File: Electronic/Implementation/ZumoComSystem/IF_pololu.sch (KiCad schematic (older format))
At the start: 4 parts, among them J3 Conn_02x13_Odd_Even, J4 Conn_02x13_Odd_Even, J5 Conn_02x07_Odd_Even, J6 Conn_02x07_Odd_Even

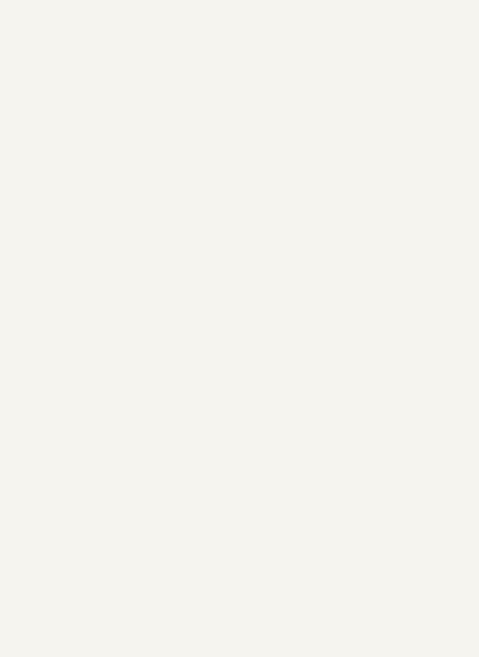
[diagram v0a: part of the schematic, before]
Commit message: electronic -> Schematic -> add hierarchical pins, modified Regulator page
           -> BOM & Clac: add new inductors
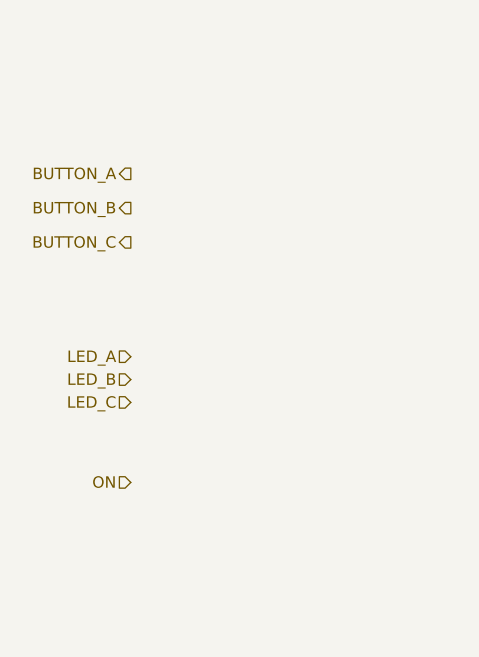
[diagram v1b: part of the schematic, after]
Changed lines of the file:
@@
 	1    0    0    -1
 $EndComp
+Text HLabel 2350 2900 0    50   Output ~ 0
+BUTTON_A
+Text HLabel 2350 3050 0    50   Output ~ 0
+BUTTON_B
+Text HLabel 2350 3200 0    50   Output ~ 0
+BUTTON_C
+Text HLabel 2350 3700 0    50   Input ~ 0
+LED_A
+Text HLabel 2350 3800 0    50   Input ~ 0
+LED_B
+Text HLabel 2350 3900 0    50   Input ~ 0
+LED_C
+Text HLabel 2350 4250 0    50   Input ~ 0
+ON
 $EndSCHEMATC

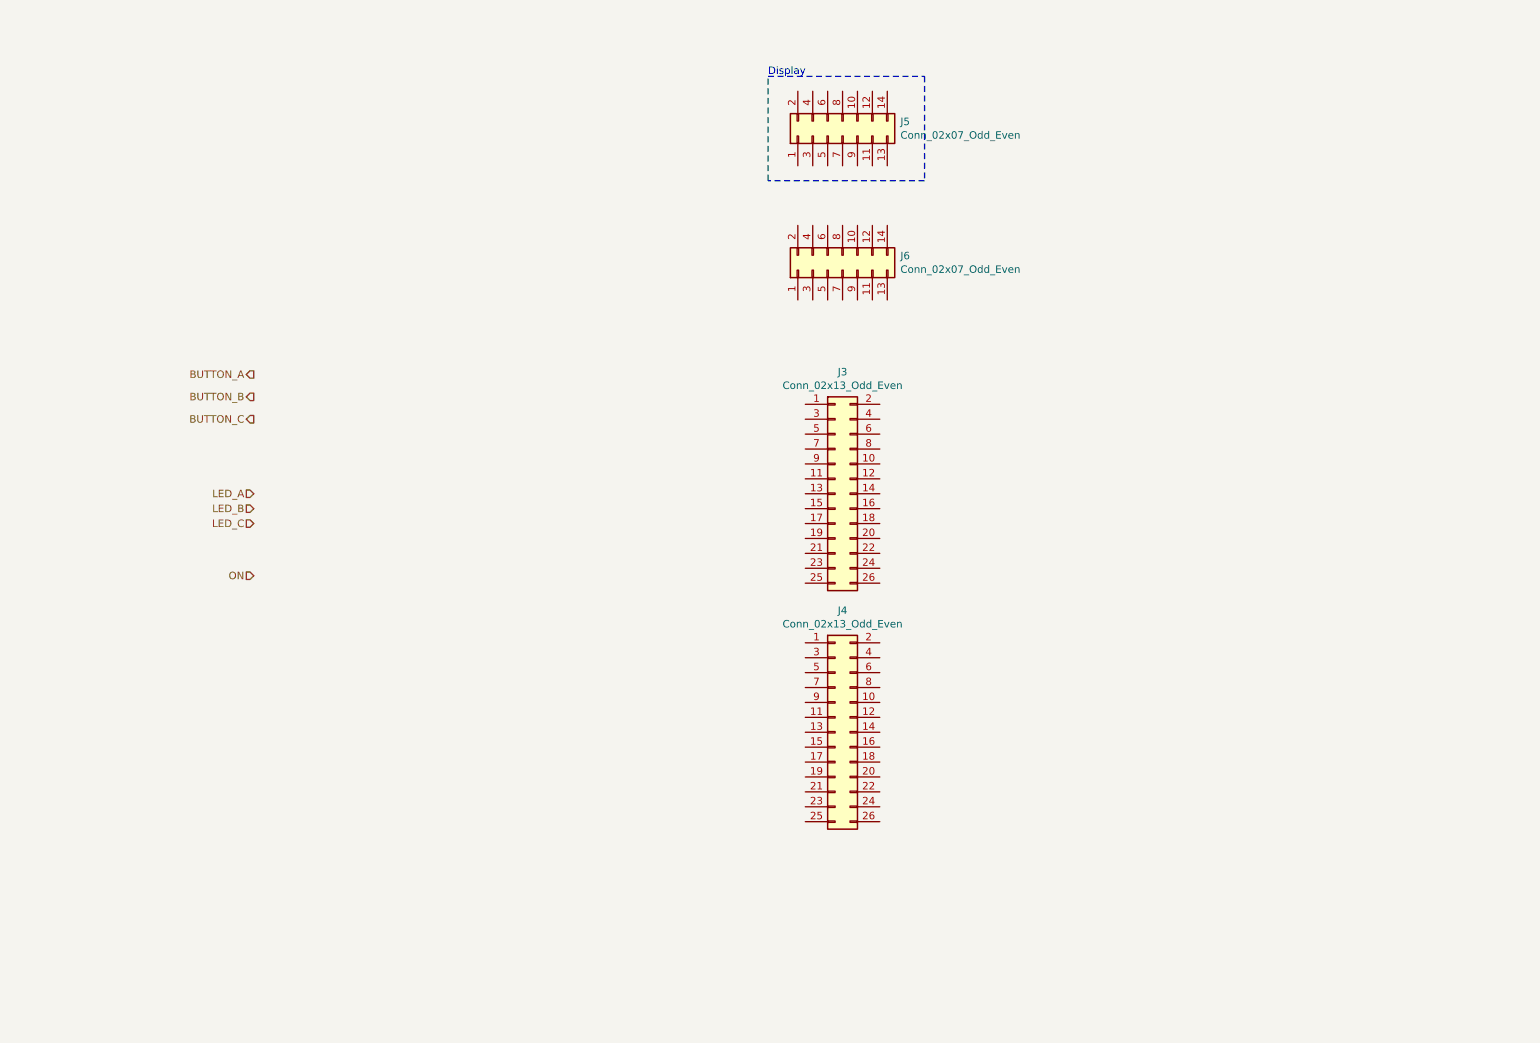
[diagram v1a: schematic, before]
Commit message: Electronic: Schematic: ESP I/Os, IF_Pololu Pins, USB_max
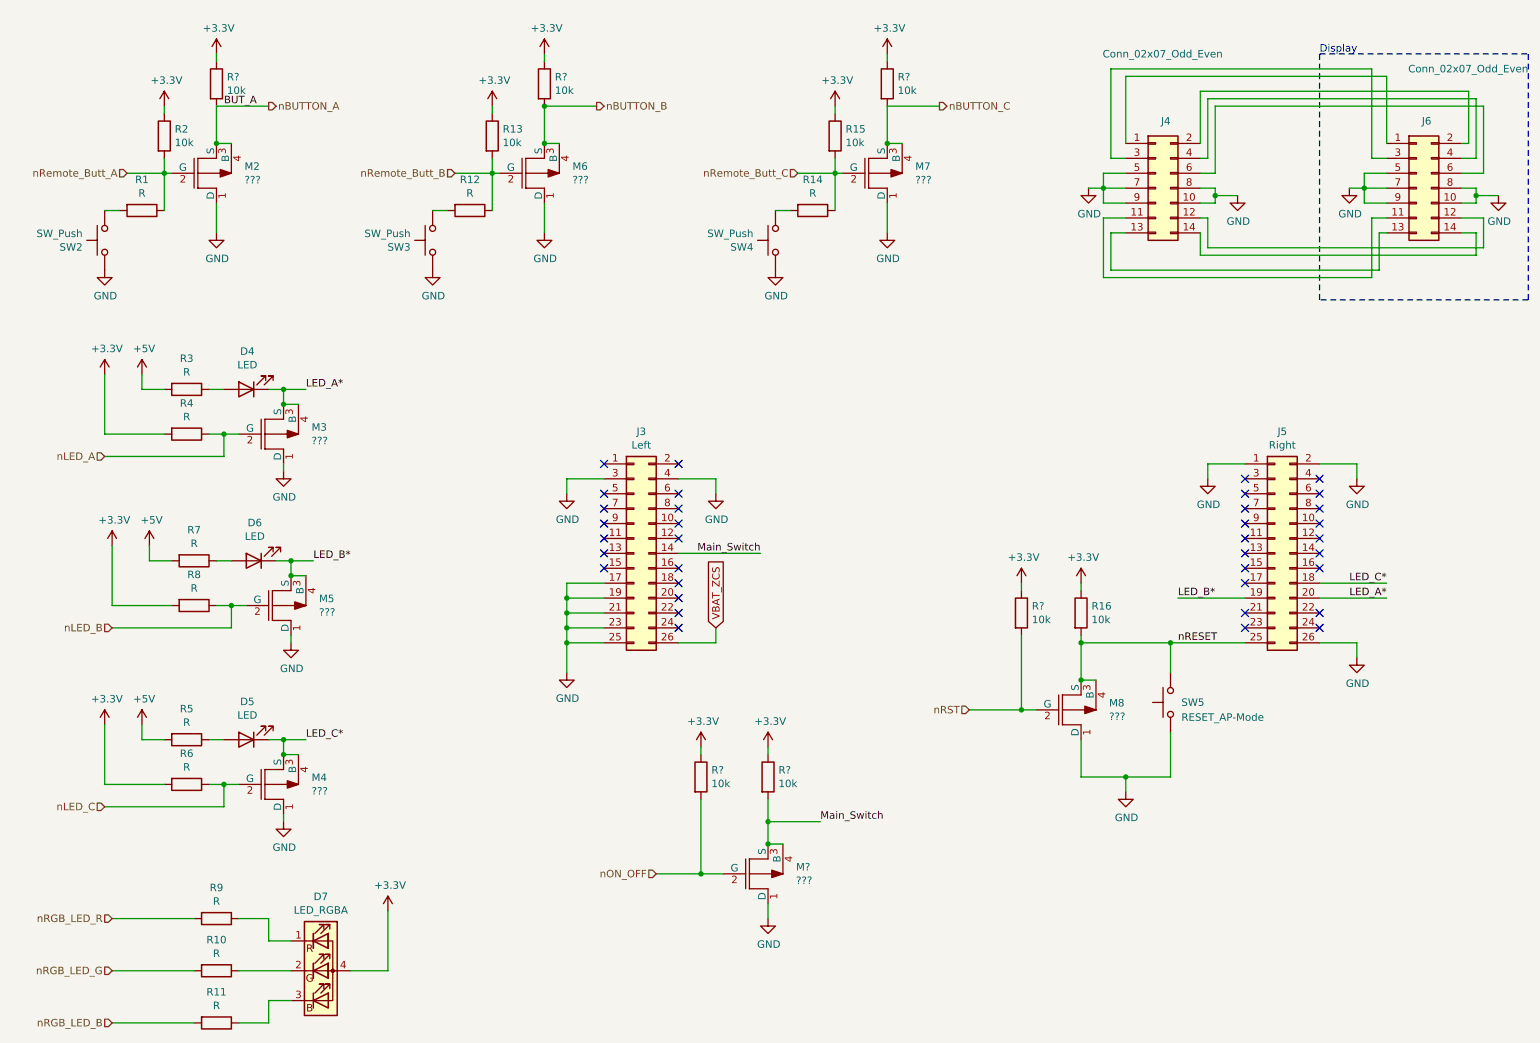
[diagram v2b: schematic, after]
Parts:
- added D4, D5, D6: LED, symbol Device:LED
- added D7: LED_RGBA, LED_SMD:LED_RGB_1210, symbol Device:LED_RGBA
- added M2, M3, M4, M5, M6, M7, M8, M?: ???, symbol pspice:MPMOS
- added R1, R10, R11, R12, R14, R3, R4, R5, R6, R7, R8, R9: R, symbol Device:R
- added R13, R15, R16, R2, R? (x6): 10k, symbol Device:R
- added SW2, SW3, SW4: SW_Push, symbol Switch:SW_Push
- added SW5: RESET_AP-Mode, Button_Switch_SMD:SW_SPST_TL3342, symbol Switch:SW_Push
- J3: value Conn_02x13_Odd_Even -> Left; footprint Connector_PinHeader_2.54mm:PinHeader_2x13_P2.54mm_Vertical -> Connector_PinHeader_2.54mm:PinHeader_2x13_P2.54mm_Vertical_SMD
- J5: renamed from J4; value Conn_02x13_Odd_Even -> Right; footprint Connector_PinHeader_2.54mm:PinHeader_2x13_P2.54mm_Vertical -> Connector_PinHeader_2.54mm:PinHeader_2x13_P2.54mm_Vertical_SMD
- renumbered J6 to J4, J5 to J6
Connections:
- net at J6.1 (Pin_1): now also J4.1 (Pin_1)
- net GND: now reaches J6.10 (Pin_10)
- net GND: now also J3.17 (Pin_17), J3.19 (Pin_19), J3.21 (Pin_21), J3.23 (Pin_23), J3.25 (Pin_25), J3.3 (Pin_3), J3.4 (Pin_4), J4.10 (Pin_10), J4.5 (Pin_5), J4.7 (Pin_7), J4.8 (Pin_8), J4.9 (Pin_9), J5.1 (Pin_1), J5.2 (Pin_2), J5.26 (Pin_26), J6.5 (Pin_5), J6.7 (Pin_7), J6.8 (Pin_8), J6.9 (Pin_9), M2.1 (D), M3.1 (D), M4.1 (D), M5.1 (D), M6.1 (D), M7.1 (D), M8.1 (D), M?.1 (D), SW2.1, SW3.1, SW4.1, SW5.1
- net at J6.11 (Pin_11): now also J4.11 (Pin_11)
- net at J6.12 (Pin_12): now also J4.12 (Pin_12)
- net at J6.13 (Pin_13): now also J4.13 (Pin_13)
- net at J6.14 (Pin_14): now also J4.14 (Pin_14)
- net at J6.2 (Pin_2): now also J4.2 (Pin_2)
- net at J6.3 (Pin_3): now also J4.3 (Pin_3)
- net at J6.4 (Pin_4): now also J4.4 (Pin_4)
- net at J6.6 (Pin_6): now also J4.6 (Pin_6)
- net Main_Switch: now reaches J3.14 (Pin_14)
- net Main_Switch: now also M?.3 (S), M?.4 (B), R?.2
- net VBAT_ZCS: now reaches J3.26 (Pin_26)
- net LED_C*: now reaches J5.18 (Pin_18)
- net LED_C*: now also D5.1 (K), M4.3 (S), M4.4 (B)
- net LED_B*: now reaches J5.19 (Pin_19)
- net LED_B*: now also D6.1 (K), M5.3 (S), M5.4 (B)
- net LED_A*: now reaches J5.20 (Pin_20)
- net LED_A*: now also D4.1 (K), M3.3 (S), M3.4 (B)
- net nRESET: now reaches J5.25 (Pin_25)
- net nRESET: now also M8.3 (S), M8.4 (B), R16.2, SW5.2
- new net: D7.1 (RK), R9.1
- new net: D7.2 (GK), R10.1
- new net: D7.3 (BK), R11.1
- new net: R12.2, SW3.2
- new net: D6.2 (A), R7.1
- new net: D4.2 (A), R3.1
- new net: R14.2, SW4.2
- new net: R1.2, SW2.2
- new net: D5.2 (A), R5.1
- new net +3V3: D7.4 (A), R13.1, R15.1, R16.1, R2.1, R4.2, R6.2, R8.2, R?.1, R?.1, R?.1, R?.1, R?.1, R?.1
- new net +5V: R3.2, R5.2, R7.2
- new net nBUTTON_A: M2.3 (S), M2.4 (B), R?.2
- new net nBUTTON_B: M6.3 (S), M6.4 (B), R?.2
- new net nBUTTON_C: M7.3 (S), M7.4 (B), R?.2
- new net nLED_A: M3.2 (G), R4.1
- new net nLED_B: M5.2 (G), R8.1
- new net nLED_C: M4.2 (G), R6.1
- new net nON_OFF: M?.2 (G), R?.2
- new net nRGB_LED_B: R11.2
- new net nRGB_LED_G: R10.2
- new net nRGB_LED_R: R9.2
- new net nRST: M8.2 (G), R?.2
- new net nRemote_Butt_A: M2.2 (G), R1.1, R2.2
- new net nRemote_Butt_B: M6.2 (G), R12.1, R13.2
- new net nRemote_Butt_C: M7.2 (G), R14.1, R15.2
- no-connect marks 0 -> 36
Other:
- moved on the sheet: J3, J4, J5, J6

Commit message: electronic: BOM: n-mosfet; SMD-pin correct position
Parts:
- removed M2, M3, M4, M5, M6, M7, M8, M?: ???, symbol pspice:MPMOS
- added Q? (x8): Q_NMOS_GDS, symbol Device:Q_NMOS_GDS
- renumbered D7 to D?, D6 to D?, D4 to D?, D5 to D?, R9 to R?, R10 to R?, R11 to R?, R16 to R?, R4 to R?, R2 to R?, R13 to R?, R15 to R?, R7 to R?, R8 to R?, R12 to R?, R14 to R?, R3 to R?, R1 to R?, R5 to R?, R6 to R?, SW5 to SW?, SW3 to SW?, SW4 to SW?, SW2 to SW?
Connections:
- net GND: now also Q?.3 (S), Q?.3 (S), Q?.3 (S), Q?.3 (S), Q?.3 (S), Q?.3 (S), Q?.3 (S), Q?.3 (S)
- net LED_A*: now also Q?.2 (D)
- net LED_B*: now also Q?.2 (D)
- net LED_C*: now also Q?.2 (D)
- net Main_Switch: now also Q?.2 (D)
- net nBUTTON_A: now also Q?.2 (D)
- net nBUTTON_B: now also Q?.2 (D)
- net nBUTTON_C: now also Q?.2 (D)
- net nLED_A: now also Q?.1 (G)
- net nLED_B: now also Q?.1 (G)
- net nLED_C: now also Q?.1 (G)
- net nON_OFF: now also Q?.1 (G)
- net nRESET: now also Q?.2 (D)
- net nRST: now also Q?.1 (G)
- net nRemote_Butt_A: now also Q?.1 (G)
- net nRemote_Butt_B: now also Q?.1 (G)
- net nRemote_Butt_C: now also Q?.1 (G)

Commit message: Electronic: nReset/AP-Mode button for ESP -> not for Zumo
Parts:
- removed SW?: RESET_AP-Mode, Button_Switch_SMD:SW_SPST_TL3342, symbol Switch:SW_Push
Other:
- moved on the sheet: Q?, R?
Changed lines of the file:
@@
 $Descr A4 11693 8268
 encoding utf-8
-Sheet 6 7
+Sheet 7 7
 Title "Zumo Communication System"
-Date "2021-07-30"
+Date "2021-08-20"
 Rev "V1.0"
 Comp "NewTec GmbH"
@@
 AR Path="/60C60623" Ref="J?"  Part="1"
 AR Path="/60C50401/60C60623" Ref="J3"  Part="1"
-F 0 "J?" H 4950 4917 50  0000 C CNN
+F 0 "J3" H 4950 4917 50  0000 C CNN
 F 1 "Left" H 4950 4826 50  0000 C CNN
 F 2 "Connector_PinHeader_2.54mm:PinHeader_2x13_P2.54mm_Vertical_SMD" H 4900 4100 50  0001 C CNN
@@
 AR Path="/60C60629" Ref="J?"  Part="1"
 AR Path="/60C50401/60C60629" Ref="J5"  Part="1"
-F 0 "J?" H 9250 4917 50  0000 C CNN
+F 0 "J5" H 9250 4917 50  0000 C CNN
 F 1 "Right" H 9250 4826 50  0000 C CNN
 F 2 "Connector_PinHeader_2.54mm:PinHeader_2x13_P2.54mm_Vertical_SMD" H 9200 4100 50  0001 C CNN
@@
 Text Label 8550 4700 0    50   ~ 0
 nRESET
-Wire Wire Line
-	7900 4950 7900 4700
-Wire Wire Line
-	7900 5350 7900 5600
 $Comp
 L power:GND #PWR?
@@
 AR Path="/60C5C844" Ref="J?"  Part="1"
 AR Path="/60C50401/60C5C844" Ref="J4"  Part="1"
-F 0 "J?" H 8500 2100 50  0000 R CNN
+F 0 "J4" H 8500 2100 50  0000 R CNN
 F 1 "Conn_02x07_Odd_Even" H 8850 2550 50  0000 R CNN
 F 2 "Connector_PinHeader_2.54mm:PinHeader_2x07_P2.54mm_Vertical" H 8400 1650 50  0001 C CNN
@@
 AR Path="/60C5C83E" Ref="J?"  Part="1"
 AR Path="/60C50401/60C5C83E" Ref="J6"  Part="1"
-F 0 "J?" H 10250 2100 50  0000 R CNN
+F 0 "J6" H 10250 2100 50  0000 R CNN
 F 1 "Conn_02x07_Odd_Even" H 10900 2450 50  0000 R CNN
 F 2 "Connector_PinSocket_2.54mm:PinSocket_2x07_P2.54mm_Vertical_SMD" H 10150 1650 50  0001 C CNN
@@
 Wire Wire Line
 	10600 1550 10450 1550
-Wire Wire Line
-	7150 5150 7500 5150
 Text Label 2700 5350 0    50   ~ 0
 LED_C*
@@
 Wire Wire Line
 	9950 4300 9500 4300
-Wire Wire Line
-	8200 5600 8200 5700
-$Comp
-L power:GND #PWR?
-U 1 1 61075918
-P 8200 5700
-F 0 "#PWR?" H 8200 5450 50  0001 C CNN
-F 1 "GND" H 8205 5527 50  0000 C CNN
-F 2 "" H 8200 5700 50  0001 C CNN
-F 3 "" H 8200 5700 50  0001 C CNN
-	1    8200 5700
-	1    0    0    -1
-$EndComp
-Wire Wire Line
-	7900 4700 8500 4700
-Wire Wire Line
-	8500 4700 8500 4900
-Wire Wire Line
-	8500 5600 8500 5300
-$Comp
-L Switch:SW_Push SW?
-U 1 1 6105C7C0
-P 8500 5100
-F 0 "SW?" V 8500 4950 50  0000 C CNN
-F 1 "RESET_AP-Mode" V 8400 4750 50  0000 C CNN
-F 2 "Button_Switch_SMD:SW_SPST_TL3342" H 8500 5300 50  0001 C CNN
-F 3 "~" H 8500 5300 50  0001 C CNN
-	1    8500 5100
-	0    -1   -1   0
-$EndComp
 $Comp
 L power:+3.3V #PWR?
 U 1 1 61030266
-P 7900 4300
-F 0 "#PWR?" H 7900 4150 50  0001 C CNN
-F 1 "+3.3V" H 7915 4473 50  0000 C CNN
-F 2 "" H 7900 4300 50  0001 C CNN
-F 3 "" H 7900 4300 50  0001 C CNN
-	1    7900 4300
-	1    0    0    -1
-$EndComp
-Wire Wire Line
-	7900 4350 7900 4300
+P 7900 4150
+F 0 "#PWR?" H 7900 4000 50  0001 C CNN
+F 1 "+3.3V" H 7915 4323 50  0000 C CNN
+F 2 "" H 7900 4150 50  0001 C CNN
+F 3 "" H 7900 4150 50  0001 C CNN
+	1    7900 4150
+	1    0    0    -1
+$EndComp
+Wire Wire Line
+	7900 4250 7900 4150
 $Comp
 L Device:R R?
 U 1 1 610325C6
-P 7900 4500
-F 0 "R?" H 7970 4546 50  0000 L CNN
-F 1 "10k" H 7970 4455 50  0000 L CNN
-F 2 "" V 7830 4500 50  0001 C CNN
-F 3 "~" H 7900 4500 50  0001 C CNN
-	1    7900 4500
-	1    0    0    -1
-$EndComp
-Connection ~ 7900 4700
-Wire Wire Line
-	7900 4650 7900 4700
-Connection ~ 8500 4700
-Wire Wire Line
-	8500 4700 9000 4700
-Connection ~ 8200 5600
-Wire Wire Line
-	8200 5600 8500 5600
-Wire Wire Line
-	7900 5600 8200 5600
+P 7900 4400
+F 0 "R?" H 7970 4446 50  0000 L CNN
+F 1 "10k" H 7970 4355 50  0000 L CNN
+F 2 "" V 7830 4400 50  0001 C CNN
+F 3 "~" H 7900 4400 50  0001 C CNN
+	1    7900 4400
+	1    0    0    -1
+$EndComp
 Text Label 9950 4400 2    50   ~ 0
 LED_A*
 Wire Wire Line
 	9500 4400 9950 4400
-Text Label 2150 1100 0    50   ~ 0
+Text Label 2150 1200 0    50   ~ 0
 BUT_A
 $Comp
@@
 Text HLabel 1400 4600 0    50   Input ~ 0
 nLED_B
-Text HLabel 6950 1100 2    50   Output ~ 0
+Text HLabel 6950 1200 2    50   Output ~ 0
 nBUTTON_C
 $Comp
@@
 Wire Wire Line
 	2150 3300 2250 3300
-Text HLabel 4650 1100 2    50   Output ~ 0
+Text HLabel 4650 1200 2    50   Output ~ 0
 nBUTTON_B
-Text HLabel 2450 1100 2    50   Output ~ 0
+Text HLabel 2450 1200 2    50   Output ~ 0
 nBUTTON_A
 Wire Wire Line
@@
 $EndComp
 Wire Wire Line
-	2100 1350 2100 1100
-Wire Wire Line
-	2100 1100 2450 1100
+	2100 1350 2100 1200
+Wire Wire Line
+	2100 1200 2450 1200
 Wire Wire Line
 	1750 1450 1750 1550
@@
 $EndComp
 Wire Wire Line
-	4300 1100 4650 1100
+	4300 1200 4650 1200
 Wire Wire Line
 	3950 1450 3950 1550
@@
 $EndComp
 Wire Wire Line
-	6600 1350 6600 1100
-Wire Wire Line
-	6600 1100 6950 1100
+	6600 1350 6600 1200
+Wire Wire Line
+	6600 1200 6950 1200
 Wire Wire Line
 	6250 1450 6250 1550
@@
 Text Label 2750 4150 0    50   ~ 0
 LED_B*
-Text HLabel 7150 5150 0    50   Input ~ 0
-nRST
 Text GLabel 5450 4600 1    50   Input ~ 0
 VBAT_ZCS
@@
 Text HLabel 5050 6250 0    50   Input ~ 0
 nON_OFF
-Text Label 6150 5900 0    50   ~ 0
-Main_Switch
 Text Label 5750 4100 2    50   ~ 0
 Main_Switch
@@
 L power:+3.3V #PWR?
 U 1 1 6196F50A
-P 7500 4300
-F 0 "#PWR?" H 7500 4150 50  0001 C CNN
-F 1 "+3.3V" H 7515 4473 50  0000 C CNN
-F 2 "" H 7500 4300 50  0001 C CNN
-F 3 "" H 7500 4300 50  0001 C CNN
-	1    7500 4300
-	1    0    0    -1
-$EndComp
-Wire Wire Line
-	7500 4350 7500 4300
+P 7500 4150
+F 0 "#PWR?" H 7500 4000 50  0001 C CNN
+F 1 "+3.3V" H 7515 4323 50  0000 C CNN
+F 2 "" H 7500 4150 50  0001 C CNN
+F 3 "" H 7500 4150 50  0001 C CNN
+	1    7500 4150
+	1    0    0    -1
+$EndComp
+Wire Wire Line
+	7500 4250 7500 4150
 $Comp
 L Device:R R?
 U 1 1 6196F511
-P 7500 4500
-F 0 "R?" H 7570 4546 50  0000 L CNN
-F 1 "10k" H 7570 4455 50  0000 L CNN
-F 2 "" V 7430 4500 50  0001 C CNN
-F 3 "~" H 7500 4500 50  0001 C CNN
-	1    7500 4500
-	1    0    0    -1
-$EndComp
-Wire Wire Line
-	7500 4650 7500 5150
-Connection ~ 7500 5150
-Wire Wire Line
-	7500 5150 7600 5150
-Wire Wire Line
-	4300 1350 4300 1100
+P 7500 4400
+F 0 "R?" H 7570 4446 50  0000 L CNN
+F 1 "10k" H 7570 4355 50  0000 L CNN
+F 2 "" V 7430 4400 50  0001 C CNN
+F 3 "~" H 7500 4400 50  0001 C CNN
+	1    7500 4400
+	1    0    0    -1
+$EndComp
+Wire Wire Line
+	4300 1350 4300 1200
 $Comp
 L power:+3.3V #PWR?
@@
 	1    0    0    -1
 $EndComp
-Connection ~ 4300 1100
 $Comp
 L power:+3.3V #PWR?
@@
 	1    0    0    -1
 $EndComp
+Wire Wire Line
+	7900 4700 9000 4700
+Connection ~ 2100 1200
+Wire Wire Line
+	2100 1200 2100 1100
+Connection ~ 4300 1200
+Wire Wire Line
+	4300 1200 4300 1100
+Connection ~ 6600 1200
+Wire Wire Line
+	6600 1200 6600 1100
+Wire Wire Line
+	7900 5200 7900 5550
 $Comp
 L Device:Q_NMOS_GDS Q?
 U 1 1 61056B48
-P 7800 5150
-F 0 "Q?" H 8004 5196 50  0000 L CNN
-F 1 "Q_NMOS_GDS" H 8004 5105 50  0000 L CNN
-F 2 "" H 8000 5250 50  0001 C CNN
-F 3 "~" H 7800 5150 50  0001 C CNN
-	1    7800 5150
-	1    0    0    -1
-$EndComp
+P 7800 5000
+F 0 "Q?" H 8004 5046 50  0000 L CNN
+F 1 "Q_NMOS_GDS" H 8004 4955 50  0000 L CNN
+F 2 "" H 8000 5100 50  0001 C CNN
+F 3 "~" H 7800 5000 50  0001 C CNN
+	1    7800 5000
+	1    0    0    -1
+$EndComp
+Wire Wire Line
+	7500 5000 7600 5000
+Connection ~ 7500 5000
+Wire Wire Line
+	7500 4550 7500 5000
+Text Label 6150 5900 0    50   ~ 0
+Main_Switch
+Text HLabel 7150 5000 0    50   Input ~ 0
+nRST
+$Comp
+L power:GND #PWR?
+U 1 1 61075918
+P 7900 5550
+F 0 "#PWR?" H 7900 5300 50  0001 C CNN
+F 1 "GND" H 7905 5377 50  0000 C CNN
+F 2 "" H 7900 5550 50  0001 C CNN
+F 3 "" H 7900 5550 50  0001 C CNN
+	1    7900 5550
+	1    0    0    -1
+$EndComp
+Wire Wire Line
+	7150 5000 7500 5000
+Wire Wire Line
+	7900 4800 7900 4700
+Wire Wire Line
+	7900 4550 7900 4700
+Connection ~ 7900 4700
 $EndSCHEMATC
